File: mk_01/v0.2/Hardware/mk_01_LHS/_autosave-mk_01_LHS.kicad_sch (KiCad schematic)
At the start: 79 parts, among them SW1 SW_Push_Dual, U1 nice_nano

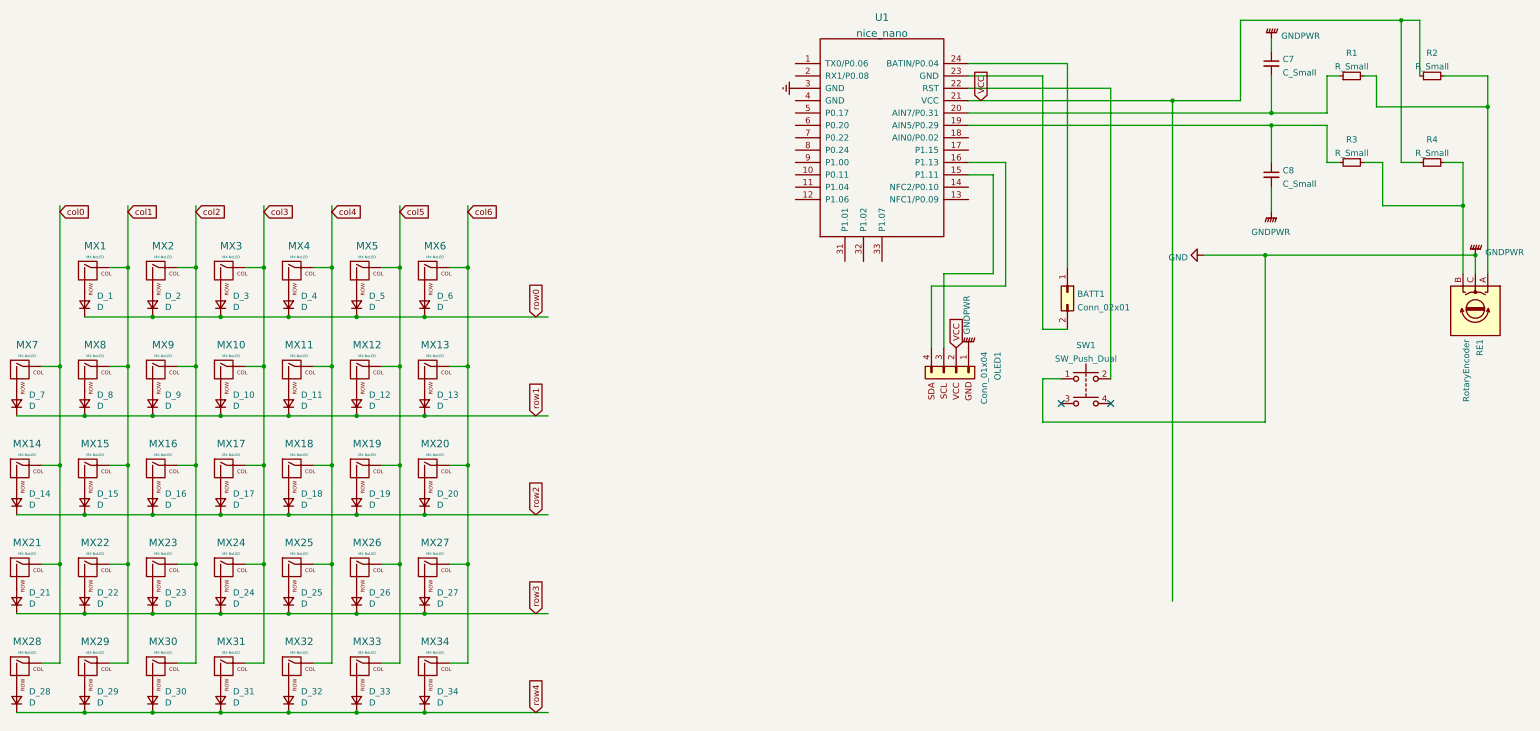
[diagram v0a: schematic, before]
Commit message: Updated PCB design
The PCB design has been updated and is now relatively complete. The hardware is fully MIT compliant, as all libraries used are under MIT license, and the design is entirely my own. Now it's time to round the tracks. The schematic has been lightly updated too based on the PCB design (changing a few connections to make routing the board simpler).
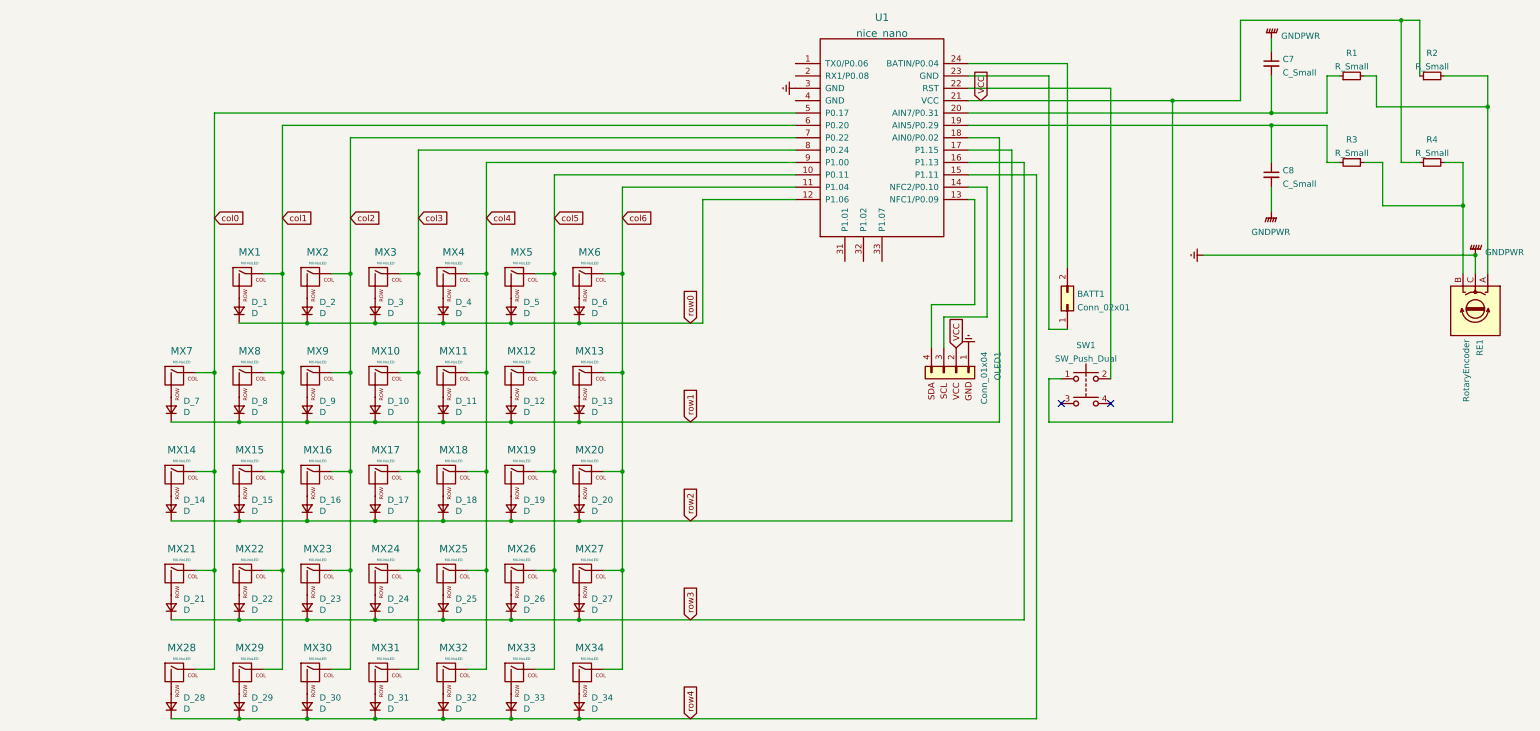
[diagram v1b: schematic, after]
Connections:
- net Earth: now also C7.1, C8.2, OLED1.1 (Pin_1), RE1.C
- net VCC: now also SW1.1
- net col0: now also U1.5 (P0.17)
- net col1: now also U1.6 (P0.20)
- net col2: now also U1.7 (P0.22)
- net col3: now also U1.8 (P0.24)
- net col4: now also U1.9 (P1.00)
- net col5: now also U1.10 (P0.11)
- net col6: now also U1.11 (P1.04)
- net row0: now also U1.12 (P1.06)
- net row1: now also U1.18 (AIN0/P0.02)
- net row2: now also U1.17 (P1.15)
- net row3: now also U1.16 (P1.13)
- net row4: now also U1.15 (P1.11)
- net at BATT1.1 (Pin_1): now also U1.23 (GND); no longer U1.24 (BATIN/P0.04)
- net at BATT1.2 (Pin_2): now also U1.24 (BATIN/P0.04); no longer U1.23 (GND)
- net at OLED1.3 (Pin_3): now also U1.14 (NFC2/P0.10); no longer U1.15 (P1.11)
- net at OLED1.4 (Pin_4): now also U1.13 (NFC1/P0.09); no longer U1.16 (P1.13)
- removed net GND: C7.1, C8.2, OLED1.1 (Pin_1), RE1.C, SW1.1
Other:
- moved on the sheet: BATT1, D_1, D_10, D_11, D_12, D_13, D_14, D_15, D_16, D_17, D_18, D_19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
